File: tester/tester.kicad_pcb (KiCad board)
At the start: 4 copper layers, 150 x 120 mm, 143 parts, among them J101 X1, J102 X3, J103 X2, J201 PWR, J202 SWD, J306 DISP, J307 SD-Card, J401 USB_B_Micro, Q201 SI2301CDS-T1-GE3, SW201 Reset, SW301 SW_Push, SW302 SW_Push, SW303 SW_Push, SW304 SW_Push, SW305 SW_Push, U101 PCA9539xPW, U102 PCA9539xPW, U201 AMS1117-3.3, U202 STM32F103C8Tx, U203 M24C64-RMN, U204 M24C64-RMN, U401 USBLC6-2SC6, U402 XC6206P332MR, U403 CH340N, Y201 8MHz, Y202 32k

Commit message: Add markings
Signed-off-by: Benedikt Spranger <b.spranger@linutronix.de>
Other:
- board text added: "☈"
- board text added: "♀"
- board text added: "♂"

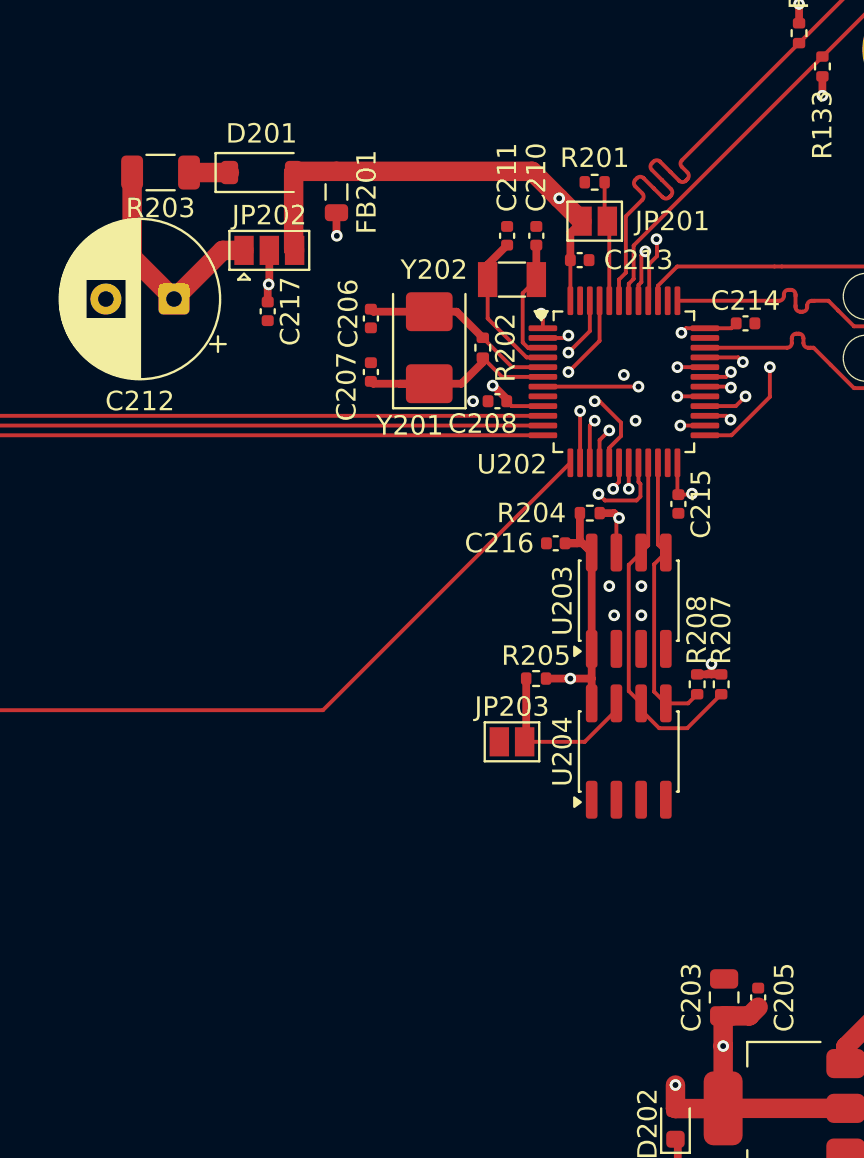
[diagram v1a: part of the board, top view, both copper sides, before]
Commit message: Add LDO recommended tantalum capacitor
Signed-off-by: Benedikt Spranger <b.spranger@linutronix.de>
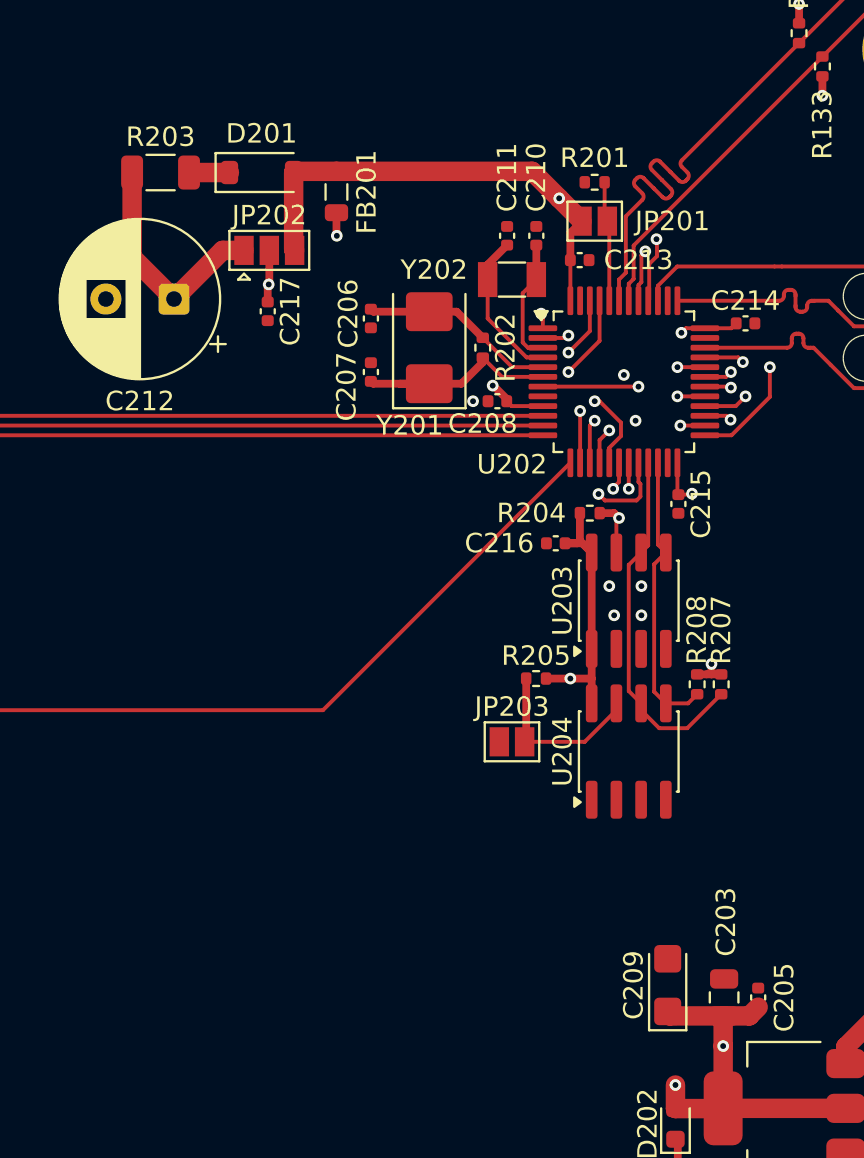
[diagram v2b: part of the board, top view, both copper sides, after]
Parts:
- added C209: 22µ, Capacitor_Tantalum_SMD:CP_EIA-3216-18_Kemet-A, F.Cu at (202.2, 131.0)
- turned R203 to 0 degrees
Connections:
- R203 pad 1: Net-(D201-K) -> /MCU/Vbat1
- R203 pad 2: /MCU/Vbat1 -> Net-(D201-K)
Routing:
- net +3V3: track 73.2 -> 76.2 mm
